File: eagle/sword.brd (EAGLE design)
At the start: 14.9 x 24.1 mm, 4 parts, among them U1 TINY45-20-DIP

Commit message: major schematic fail...
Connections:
- new net N$1: J1.1, S1.4
- net GND: no longer S1.3
- net VCC: no longer J1.1
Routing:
- net VCC: track 34.1 -> 2.87 mm
- net N$1: track 0.00 -> 28.5 mm
- net GND: track 7.80 -> 27.9 mm
- net DIN: track 11.1 -> 11.7 mm
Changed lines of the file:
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@@
 <?xml version="1.0" encoding="utf-8"?>
 <!DOCTYPE eagle SYSTEM "eagle.dtd">
-<eagle version="7.5.0">
+<eagle version="8.0.0">
 <drawing>
 <settings>
@@
 <setting verticaltext="up"/>
 </settings>
-<grid distance="0.0001" unitdist="inch" unit="inch" style="lines" multiple="1" display="no" altdistance="0.025" altunitdist="inch" altunit="inch"/>
+<grid distance="0.025" unitdist="inch" unit="inch" style="lines" multiple="1" display="no" altdistance="0.025" altunitdist="inch" altunit="inch"/>
 <layers>
 <layer number="1" name="Top" color="4" fill="1" visible="yes" active="yes"/>
@@
 <contactref element="U1" pad="8"/>
 <contactref element="S1" pad="2"/>
-<contactref element="J1" pad="1"/>
-<wire x1="3.81" y1="2.54" x2="1.27" y2="2.54" width="1.27" layer="16"/>
-<wire x1="1.27" y1="2.54" x2="1.27" y2="12.7" width="1.27" layer="16"/>
-<wire x1="1.27" y1="12.7" x2="3.81" y2="12.7" width="1.27" layer="16"/>
-<wire x1="1.27" y1="15.5194" x2="1.27" y2="22.86" width="1.27" layer="16"/>
-<wire x1="1.27" y1="22.86" x2="6.23061875" y2="22.86" width="1.27" layer="16"/>
-<wire x1="4.3688" y1="15.5194" x2="1.27" y2="15.5194" width="1.27" layer="16"/>
-<wire x1="1.27" y1="12.7" x2="1.27" y2="15.5194" width="1.27" layer="16"/>
-<wire x1="6.23061875" y1="22.86" x2="6.23061875" y2="23.4569" width="1.27" layer="16"/>
-<wire x1="6.23061875" y1="23.4569" x2="6.1976" y2="24.13" width="0" layer="19" extent="1-16"/>
+<wire x1="3.81" y1="12.7" x2="4.3688" y2="15.5194" width="0.8128" layer="16"/>
 </signal>
 <signal name="GND">
 <contactref element="U1" pad="4"/>
-<contactref element="S1" pad="3"/>
 <contactref element="J2" pad="1"/>
-<wire x1="11.43" y1="5.08" x2="11.43" y2="2.54" width="1.27" layer="16"/>
 <polygon width="1.27" layer="16" thermals="no">
 <vertex x="0" y="24.765"/>
@@
 <vertex x="-0.635" y="24.765"/>
 </polygon>
-<wire x1="10.8712" y1="20.0406" x2="9.0297" y2="20.0406" width="1.27" layer="16"/>
-<wire x1="9.0297" y1="20.0406" x2="9.0297" y2="23.4569" width="1.27" layer="16"/>
-<wire x1="9.0297" y1="23.4569" x2="9.0424" y2="24.13" width="0" layer="19" extent="1-16"/>
+<wire x1="11.43" y1="2.54" x2="13.335" y2="2.54" width="0.8128" layer="16"/>
+<wire x1="13.335" y1="2.54" x2="13.335" y2="22.225" width="0.8128" layer="16"/>
+<wire x1="13.335" y1="22.225" x2="8.89" y2="22.225" width="0.8128" layer="16"/>
+<wire x1="8.89" y1="22.225" x2="8.89" y2="24.13" width="0.8128" layer="16"/>
 </signal>
 <signal name="DIN">
 <contactref element="U1" pad="7"/>
-<wire x1="6.35" y1="12.7" x2="7.62" y2="15.24" width="1.27" layer="16"/>
-<wire x1="7.62" y1="15.24" x2="7.62" y2="23.495" width="1.27" layer="16"/>
-<wire x1="7.62" y1="23.495" x2="7.62" y2="24.13" width="0" layer="19" extent="1-16"/>
+<wire x1="6.35" y1="12.7" x2="7.62" y2="15.24" width="0.8128" layer="16"/>
+<wire x1="7.62" y1="15.24" x2="7.62" y2="24.13" width="0.8128" layer="16"/>
+</signal>
+<signal name="N$1">
+<contactref element="J1" pad="1"/>
+<contactref element="S1" pad="4"/>
+<wire x1="3.81" y1="2.54" x2="1.905" y2="2.54" width="0.8128" layer="16"/>
+<wire x1="1.905" y1="2.54" x2="1.905" y2="20.32" width="0.8128" layer="16"/>
+<wire x1="1.905" y1="20.32" x2="4.3688" y2="20.32" width="0.8128" layer="16"/>
+<wire x1="4.3688" y1="20.32" x2="4.3688" y2="20.0406" width="0.8128" layer="16"/>
+<wire x1="4.3688" y1="20.0406" x2="6.35" y2="20.0406" width="0.8128" layer="16"/>
+<wire x1="6.35" y1="20.0406" x2="6.35" y2="24.13" width="0.8128" layer="16"/>
 </signal>
 </signals>

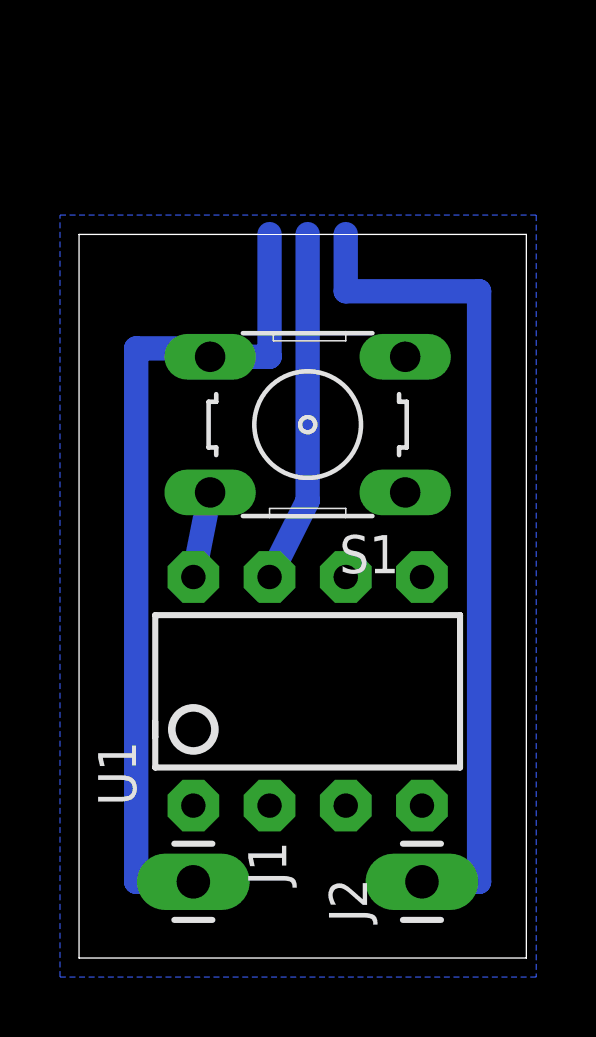
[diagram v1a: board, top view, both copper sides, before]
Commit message: fixed button spacing
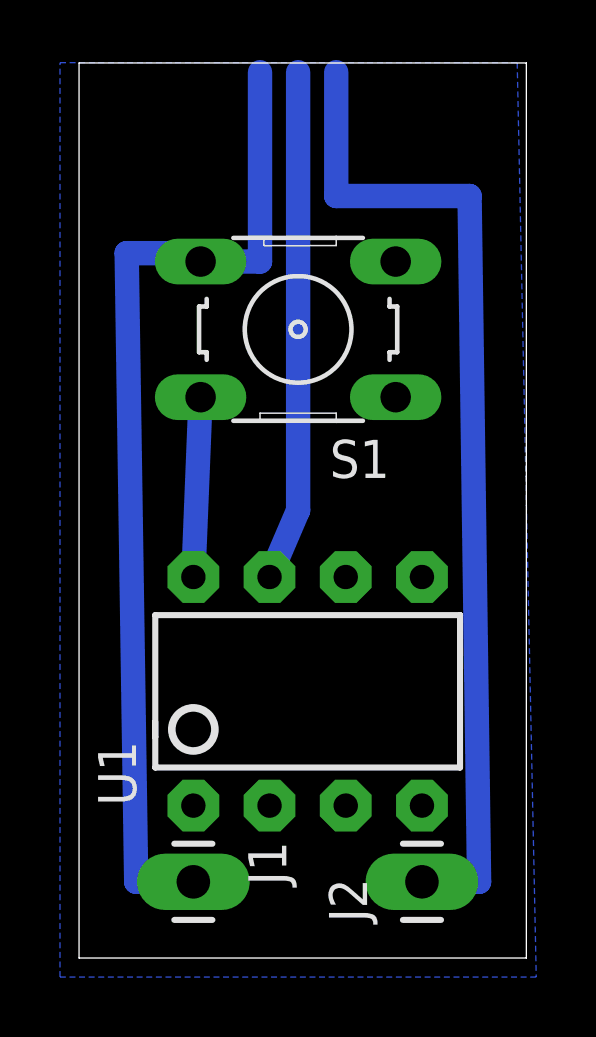
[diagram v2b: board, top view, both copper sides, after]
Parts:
- moved S1 3.19 mm to (7.30, 21.0)
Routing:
- net N$1: track 28.5 -> 33.9 mm
- net GND: track 27.9 -> 33.3 mm
- net DIN: track 11.7 -> 17.0 mm
- net VCC: track 2.87 -> 6.00 mm
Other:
- board size 14.9 x 24.1 mm -> 14.9 x 29.8 mm
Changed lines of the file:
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@@
 <setting verticaltext="up"/>
 </settings>
-<grid distance="0.025" unitdist="inch" unit="inch" style="lines" multiple="1" display="no" altdistance="0.025" altunitdist="inch" altunit="inch"/>
+<grid distance="0.0125" unitdist="inch" unit="inch" style="lines" multiple="1" display="no" altdistance="0.025" altunitdist="inch" altunit="inch"/>
 <layers>
 <layer number="1" name="Top" color="4" fill="1" visible="yes" active="yes"/>
@@
 <plain>
 <wire x1="0" y1="0" x2="14.91" y2="0" width="0" layer="20"/>
-<wire x1="14.91" y1="0" x2="14.91" y2="24.12" width="0" layer="20"/>
-<wire x1="14.91" y1="24.12" x2="0" y2="24.12" width="0" layer="20"/>
-<wire x1="0" y1="24.12" x2="0" y2="0" width="0" layer="20"/>
+<wire x1="14.91" y1="0" x2="14.91" y2="29.835" width="0" layer="20"/>
+<wire x1="14.91" y1="29.835" x2="0" y2="29.835" width="0" layer="20"/>
+<wire x1="0" y1="29.835" x2="0" y2="0" width="0" layer="20"/>
 </plain>
 <attributes>
@@
 <element name="J1" library="SparkFun-Connectors" package="1X01_LONGPAD" value="" x="3.81" y="2.54" rot="R270"/>
 <element name="J2" library="SparkFun-Connectors" package="1X01_LONGPAD" value="" x="11.43" y="2.54" rot="R90"/>
-<element name="S1" library="switch-omron" package="B3F-10XX" value="" x="7.62" y="17.78" rot="R180">
-<attribute name="OC_NEWARK" value="36M3542" x="7.62" y="17.78" size="1.778" layer="27" rot="R180" display="off"/>
-<attribute name="MF" value="" x="7.62" y="17.78" size="1.778" layer="27" rot="R180" display="off"/>
-<attribute name="MPN" value="B3F-1000" x="7.62" y="17.78" size="1.778" layer="27" rot="R180" display="off"/>
-<attribute name="OC_FARNELL" value="176432" x="7.62" y="17.78" size="1.778" layer="27" rot="R180" display="off"/>
+<element name="S1" library="switch-omron" package="B3F-10XX" value="" x="7.3025" y="20.955" rot="R180">
+<attribute name="OC_NEWARK" value="36M3542" x="7.3025" y="20.955" size="1.778" layer="27" rot="R180" display="off"/>
+<attribute name="MF" value="" x="7.3025" y="20.955" size="1.778" layer="27" rot="R180" display="off"/>
+<attribute name="MPN" value="B3F-1000" x="7.3025" y="20.955" size="1.778" layer="27" rot="R180" display="off"/>
+<attribute name="OC_FARNELL" value="176432" x="7.3025" y="20.955" size="1.778" layer="27" rot="R180" display="off"/>
 </element>
 <element name="U1" library="SparkFun-DigitalIC" package="DIP08" value="TINY45-20-DIP" x="7.62" y="8.89">
@@
 <contactref element="U1" pad="8"/>
 <contactref element="S1" pad="2"/>
-<wire x1="3.81" y1="12.7" x2="4.3688" y2="15.5194" width="0.8128" layer="16"/>
+<wire x1="3.81" y1="12.7" x2="4.0513" y2="18.6944" width="0.8128" layer="16"/>
 </signal>
 <signal name="GND">
@@
 <contactref element="J2" pad="1"/>
 <polygon width="1.27" layer="16" thermals="no">
-<vertex x="0" y="24.765"/>
-<vertex x="15.24" y="24.765"/>
+<vertex x="-0.635" y="29.845"/>
+<vertex x="14.605" y="29.845"/>
 <vertex x="15.24" y="-0.635"/>
 <vertex x="-0.635" y="-0.635"/>
-<vertex x="-0.635" y="24.765"/>
 </polygon>
 <wire x1="11.43" y1="2.54" x2="13.335" y2="2.54" width="0.8128" layer="16"/>
-<wire x1="13.335" y1="2.54" x2="13.335" y2="22.225" width="0.8128" layer="16"/>
-<wire x1="13.335" y1="22.225" x2="8.89" y2="22.225" width="0.8128" layer="16"/>
-<wire x1="8.89" y1="22.225" x2="8.89" y2="24.13" width="0.8128" layer="16"/>
+<wire x1="13.335" y1="2.54" x2="13.0175" y2="25.4" width="0.8128" layer="16"/>
+<wire x1="13.0175" y1="25.4" x2="8.5725" y2="25.4" width="0.8128" layer="16"/>
+<wire x1="8.5725" y1="25.4" x2="8.5725" y2="29.5275" width="0.8128" layer="16"/>
 </signal>
 <signal name="DIN">
 <contactref element="U1" pad="7"/>
-<wire x1="6.35" y1="12.7" x2="7.62" y2="15.24" width="0.8128" layer="16"/>
-<wire x1="7.62" y1="15.24" x2="7.62" y2="24.13" width="0.8128" layer="16"/>
+<wire x1="6.35" y1="12.7" x2="7.3025" y2="14.9225" width="0.8128" layer="16"/>
+<wire x1="7.3025" y1="14.9225" x2="7.3025" y2="29.5275" width="0.8128" layer="16"/>
 </signal>
 <signal name="N$1">
@@
 <contactref element="S1" pad="4"/>
 <wire x1="3.81" y1="2.54" x2="1.905" y2="2.54" width="0.8128" layer="16"/>
-<wire x1="1.905" y1="2.54" x2="1.905" y2="20.32" width="0.8128" layer="16"/>
-<wire x1="1.905" y1="20.32" x2="4.3688" y2="20.32" width="0.8128" layer="16"/>
-<wire x1="4.3688" y1="20.32" x2="4.3688" y2="20.0406" width="0.8128" layer="16"/>
-<wire x1="4.3688" y1="20.0406" x2="6.35" y2="20.0406" width="0.8128" layer="16"/>
-<wire x1="6.35" y1="20.0406" x2="6.35" y2="24.13" width="0.8128" layer="16"/>
+<wire x1="1.905" y1="2.54" x2="1.5875" y2="23.495" width="0.8128" layer="16"/>
+<wire x1="1.5875" y1="23.495" x2="4.0513" y2="23.495" width="0.8128" layer="16"/>
+<wire x1="4.0513" y1="23.495" x2="4.0513" y2="23.2156" width="0.8128" layer="16"/>
+<wire x1="4.0513" y1="23.2156" x2="6.0325" y2="23.2156" width="0.8128" layer="16"/>
+<wire x1="6.0325" y1="23.2156" x2="6.0325" y2="29.5275" width="0.8128" layer="16"/>
 </signal>
 </signals>

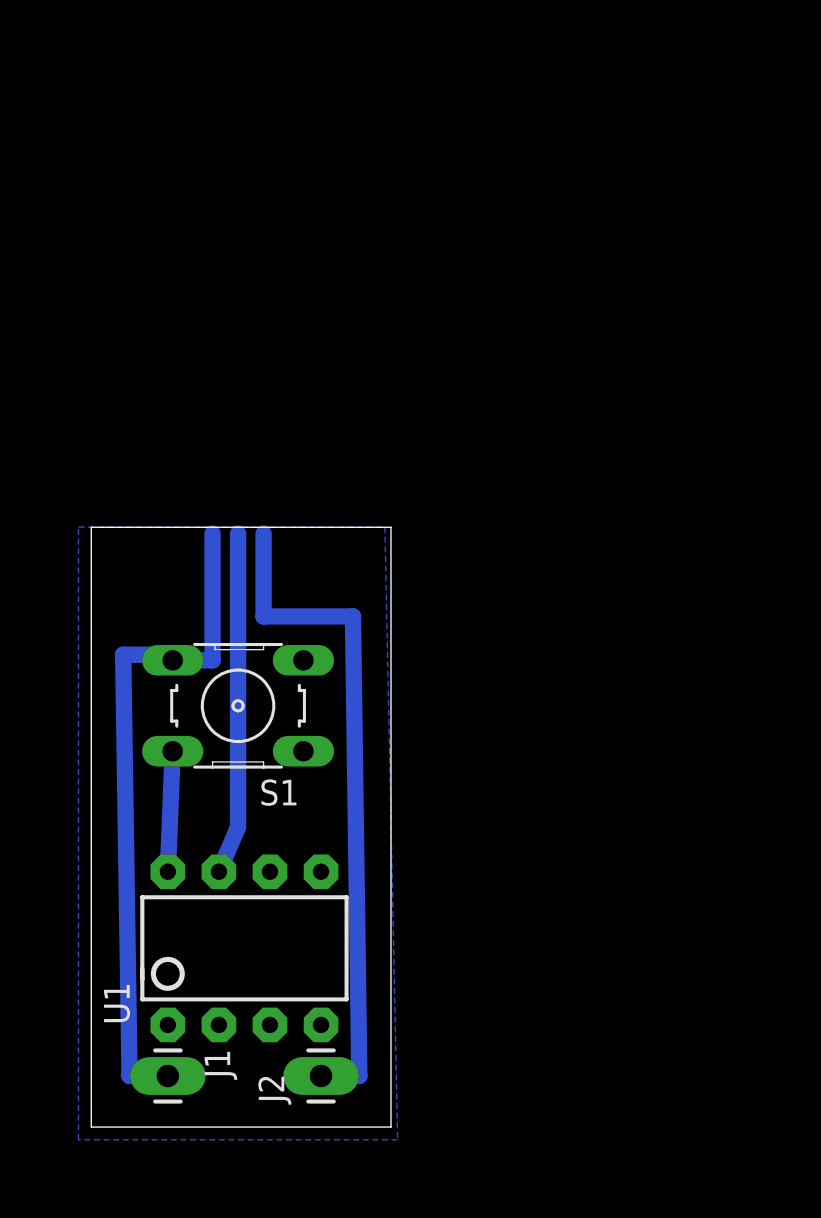
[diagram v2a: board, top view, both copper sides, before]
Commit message: added battery "connector"
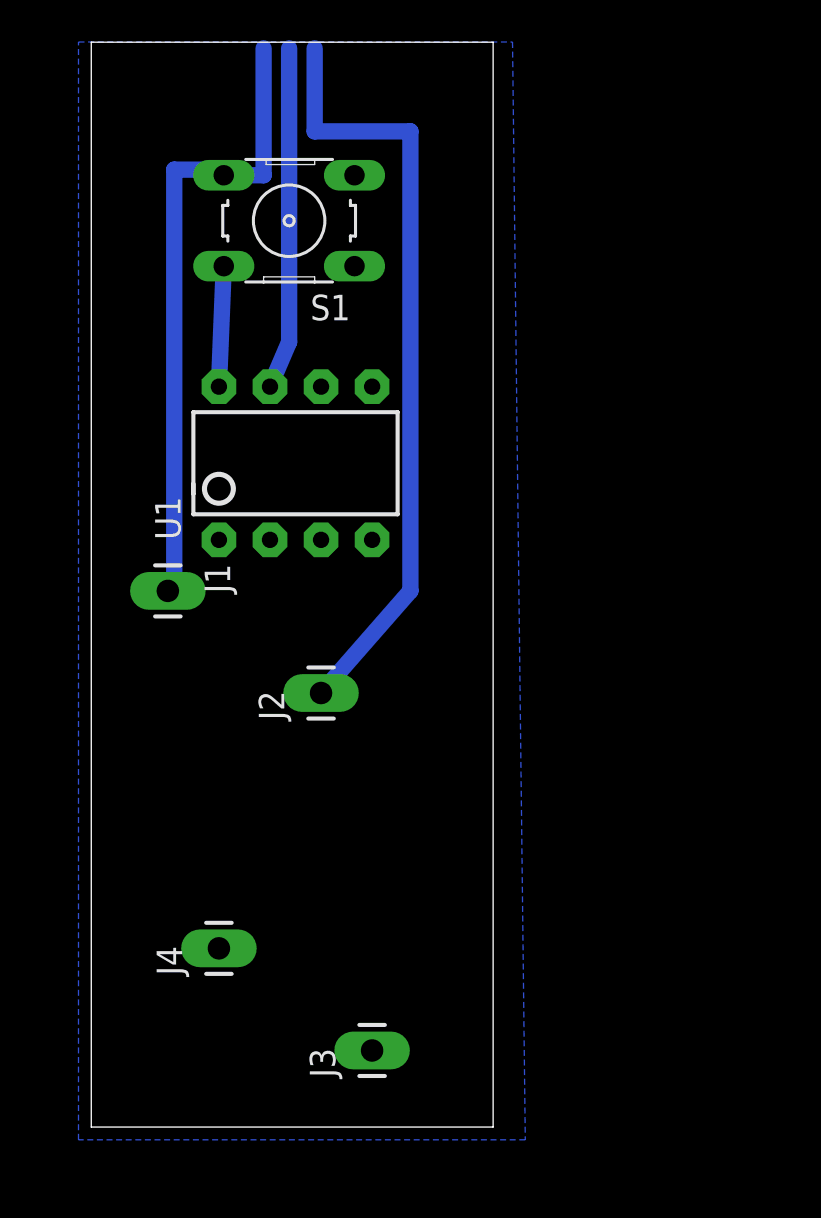
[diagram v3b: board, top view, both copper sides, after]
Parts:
- added J3, J4: (no value), SparkFun-Connectors:1X01_LONGPAD
- moved S1 24.3 mm to (9.84, 45.1)
- moved U1 24.3 mm to (10.2, 33.0)
- moved J1 24.1 mm to (3.81, 26.7)
- moved J2 19.1 mm to (11.4, 21.6)
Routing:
- net GND: track 33.3 -> 38.5 mm
- net N$1: track 33.9 -> 32.3 mm
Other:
- board size 14.9 x 29.8 mm -> 20 x 54 mm
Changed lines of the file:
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@@
 <setting verticaltext="up"/>
 </settings>
-<grid distance="0.0125" unitdist="inch" unit="inch" style="lines" multiple="1" display="no" altdistance="0.025" altunitdist="inch" altunit="inch"/>
+<grid distance="0.1" unitdist="inch" unit="inch" style="lines" multiple="1" display="no" altdistance="0.025" altunitdist="inch" altunit="inch"/>
 <layers>
 <layer number="1" name="Top" color="4" fill="1" visible="yes" active="yes"/>
@@
 <board>
 <plain>
-<wire x1="0" y1="0" x2="14.91" y2="0" width="0" layer="20"/>
-<wire x1="14.91" y1="0" x2="14.91" y2="29.835" width="0" layer="20"/>
-<wire x1="14.91" y1="29.835" x2="0" y2="29.835" width="0" layer="20"/>
-<wire x1="0" y1="29.835" x2="0" y2="0" width="0" layer="20"/>
+<wire x1="0" y1="0" x2="19.99" y2="0" width="0" layer="20"/>
+<wire x1="19.99" y1="0" x2="19.99" y2="53.965" width="0" layer="20"/>
+<wire x1="19.99" y1="53.965" x2="0" y2="53.965" width="0" layer="20"/>
+<wire x1="0" y1="53.965" x2="0" y2="0" width="0" layer="20"/>
 </plain>
 <attributes>
@@
 </autorouter>
 <elements>
-<element name="J1" library="SparkFun-Connectors" package="1X01_LONGPAD" value="" x="3.81" y="2.54" rot="R270"/>
-<element name="J2" library="SparkFun-Connectors" package="1X01_LONGPAD" value="" x="11.43" y="2.54" rot="R90"/>
-<element name="S1" library="switch-omron" package="B3F-10XX" value="" x="7.3025" y="20.955" rot="R180">
-<attribute name="OC_NEWARK" value="36M3542" x="7.3025" y="20.955" size="1.778" layer="27" rot="R180" display="off"/>
-<attribute name="MF" value="" x="7.3025" y="20.955" size="1.778" layer="27" rot="R180" display="off"/>
-<attribute name="MPN" value="B3F-1000" x="7.3025" y="20.955" size="1.778" layer="27" rot="R180" display="off"/>
-<attribute name="OC_FARNELL" value="176432" x="7.3025" y="20.955" size="1.778" layer="27" rot="R180" display="off"/>
+<element name="J1" library="SparkFun-Connectors" package="1X01_LONGPAD" value="" x="3.81" y="26.67" rot="R270"/>
+<element name="J2" library="SparkFun-Connectors" package="1X01_LONGPAD" value="" x="11.43" y="21.59" rot="R90"/>
+<element name="S1" library="switch-omron" package="B3F-10XX" value="" x="9.8425" y="45.085" rot="R180">
+<attribute name="OC_NEWARK" value="36M3542" x="9.8425" y="45.085" size="1.778" layer="27" rot="R180" display="off"/>
+<attribute name="MF" value="" x="9.8425" y="45.085" size="1.778" layer="27" rot="R180" display="off"/>
+<attribute name="MPN" value="B3F-1000" x="9.8425" y="45.085" size="1.778" layer="27" rot="R180" display="off"/>
+<attribute name="OC_FARNELL" value="176432" x="9.8425" y="45.085" size="1.778" layer="27" rot="R180" display="off"/>
 </element>
-<element name="U1" library="SparkFun-DigitalIC" package="DIP08" value="TINY45-20-DIP" x="7.62" y="8.89">
-<attribute name="PROD_ID" value="IC-09439" x="7.62" y="8.89" size="1.778" layer="27" display="off"/>
+<element name="U1" library="SparkFun-DigitalIC" package="DIP08" value="TINY45-20-DIP" x="10.16" y="33.02">
+<attribute name="PROD_ID" value="IC-09439" x="10.16" y="33.02" size="1.778" layer="27" display="off"/>
 </element>
+<element name="J3" library="SparkFun-Connectors" package="1X01_LONGPAD" value="" x="13.97" y="3.81" rot="R90"/>
+<element name="J4" library="SparkFun-Connectors" package="1X01_LONGPAD" value="" x="6.35" y="8.89" rot="R90"/>
 </elements>
 <signals>
@@
 <contactref element="U1" pad="8"/>
 <contactref element="S1" pad="2"/>
-<wire x1="3.81" y1="12.7" x2="4.0513" y2="18.6944" width="0.8128" layer="16"/>
+<wire x1="6.35" y1="36.83" x2="6.5913" y2="42.8244" width="0.8128" layer="16"/>
 </signal>
 <signal name="GND">
@@
 <contactref element="J2" pad="1"/>
 <polygon width="1.27" layer="16" thermals="no">
-<vertex x="-0.635" y="29.845"/>
-<vertex x="14.605" y="29.845"/>
-<vertex x="15.24" y="-0.635"/>
+<vertex x="-0.635" y="53.975"/>
+<vertex x="20.955" y="53.975"/>
+<vertex x="21.59" y="-0.635"/>
 <vertex x="-0.635" y="-0.635"/>
 </polygon>
-<wire x1="11.43" y1="2.54" x2="13.335" y2="2.54" width="0.8128" layer="16"/>
-<wire x1="13.335" y1="2.54" x2="13.0175" y2="25.4" width="0.8128" layer="16"/>
-<wire x1="13.0175" y1="25.4" x2="8.5725" y2="25.4" width="0.8128" layer="16"/>
-<wire x1="8.5725" y1="25.4" x2="8.5725" y2="29.5275" width="0.8128" layer="16"/>
+<wire x1="11.43" y1="21.59" x2="15.875" y2="26.67" width="0.8128" layer="16"/>
+<wire x1="15.875" y1="26.67" x2="15.875" y2="49.53" width="0.8128" layer="16"/>
+<wire x1="15.875" y1="49.53" x2="11.1125" y2="49.53" width="0.8128" layer="16"/>
+<wire x1="11.1125" y1="49.53" x2="11.1125" y2="53.6575" width="0.8128" layer="16"/>
+<wire x1="11.43" y1="21.59" x2="13.97" y2="29.21" width="0" layer="19" extent="1-1"/>
 </signal>
 <signal name="DIN">
 <contactref element="U1" pad="7"/>
-<wire x1="6.35" y1="12.7" x2="7.3025" y2="14.9225" width="0.8128" layer="16"/>
-<wire x1="7.3025" y1="14.9225" x2="7.3025" y2="29.5275" width="0.8128" layer="16"/>
+<wire x1="8.89" y1="36.83" x2="9.8425" y2="39.0525" width="0.8128" layer="16"/>
+<wire x1="9.8425" y1="39.0525" x2="9.8425" y2="53.6575" width="0.8128" layer="16"/>
 </signal>
 <signal name="N$1">
 <contactref element="J1" pad="1"/>
 <contactref element="S1" pad="4"/>
-<wire x1="3.81" y1="2.54" x2="1.905" y2="2.54" width="0.8128" layer="16"/>
-<wire x1="1.905" y1="2.54" x2="1.5875" y2="23.495" width="0.8128" layer="16"/>
-<wire x1="1.5875" y1="23.495" x2="4.0513" y2="23.495" width="0.8128" layer="16"/>
-<wire x1="4.0513" y1="23.495" x2="4.0513" y2="23.2156" width="0.8128" layer="16"/>
-<wire x1="4.0513" y1="23.2156" x2="6.0325" y2="23.2156" width="0.8128" layer="16"/>
-<wire x1="6.0325" y1="23.2156" x2="6.0325" y2="29.5275" width="0.8128" layer="16"/>
+<wire x1="3.81" y1="26.67" x2="4.1275" y2="26.67" width="0.8128" layer="16"/>
+<wire x1="4.1275" y1="26.67" x2="4.1275" y2="47.625" width="0.8128" layer="16"/>
+<wire x1="4.1275" y1="47.625" x2="6.5913" y2="47.625" width="0.8128" layer="16"/>
+<wire x1="6.5913" y1="47.625" x2="6.5913" y2="47.3456" width="0.8128" layer="16"/>
+<wire x1="6.5913" y1="47.3456" x2="8.5725" y2="47.3456" width="0.8128" layer="16"/>
+<wire x1="8.5725" y1="47.3456" x2="8.5725" y2="53.6575" width="0.8128" layer="16"/>
 </signal>
 </signals>
